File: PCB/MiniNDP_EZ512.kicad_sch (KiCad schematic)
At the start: 16 parts, among them J1 Conn_02x20_Odd_Even, U1 HC238, U2 HC4040, U3 FCT841, U4 AS6C4008, U5 HC00

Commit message: polish EZ512
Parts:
- C4: value 1u -> 47u; MPN CL31B105KAHNNNE -> C3216X5R1E476M160DC
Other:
- note added: "512K easy build"
- note removed: "NOT TESTED 512K easy build"
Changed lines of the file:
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@@
 	)
 	(junction
-		(at 119.38 162.56)
-		(diameter 0)
-		(color 0 0 0 0)
-	)
-	(junction
 		(at 127 147.32)
 		(diameter 0)
@@
 	)
 	(junction
+		(at 119.38 162.56)
+		(diameter 0)
+		(color 0 0 0 0)
+	)
+	(junction
 		(at 107.95 36.83)
 		(diameter 0)
@@
 	(wire
 		(pts
+			(xy 119.38 162.56) (xy 125.73 162.56)
+		)
+		(stroke
+			(width 0)
+			(type default)
+		)
+	)
+	(wire
+		(pts
 			(xy 34.29 41.91) (xy 44.45 41.91)
 		)
@@
 	(wire
 		(pts
-			(xy 114.3 167.64) (xy 119.38 167.64)
-		)
-		(stroke
-			(width 0)
-			(type default)
-		)
-	)
-	(wire
-		(pts
 			(xy 205.74 55.88) (xy 215.9 55.88)
 		)
@@
 		)
 	)
-	(wire
-		(pts
-			(xy 119.38 162.56) (xy 125.73 162.56)
-		)
-		(stroke
-			(width 0)
-			(type default)
-		)
-	)
 	(bus
 		(pts
@@
 	(wire
 		(pts
+			(xy 119.38 167.64) (xy 125.73 167.64)
+		)
+		(stroke
+			(width 0)
+			(type default)
+		)
+	)
+	(wire
+		(pts
 			(xy 241.3 68.58) (xy 257.81 68.58)
 		)
@@
 	(wire
 		(pts
-			(xy 119.38 167.64) (xy 125.73 167.64)
+			(xy 114.3 167.64) (xy 119.38 167.64)
 		)
 		(stroke
@@
 		)
 	)
-	(text "NOT TESTED\n512K easy build"
+	(text "512K easy build"
 		(exclude_from_sim no)
 		(at 261.112 173.99 0)
@@
 	)
 	(symbol
-		(lib_id "000_LOCAL:C")
-		(at 119.38 165.1 0)
-		(unit 1)
-		(exclude_from_sim no)
-		(in_bom yes)
-		(on_board yes)
-		(dnp no)
-		(property "Reference" "C4"
-			(at 119.38 158.75 0)
-			(effects
-				(font
-					(size 1.27 1.27)
-				)
-			)
-		)
-		(property "Value" "1u"
-			(at 119.38 161.036 0)
-			(effects
-				(font
-					(size 1.27 1.27)
-				)
-			)
-		)
-		(property "Footprint" "000_LOCAL:C_1206"
-			(at 119.38 165.1 0)
-			(effects
-				(font
-					(size 1.27 1.27)
-				)
-				(hide yes)
-			)
-		)
-		(property "Datasheet" "datasheets/CL05Y105KP6VPN.pdf"
-			(at 119.38 165.1 0)
-			(effects
-				(font
-					(size 1.27 1.27)
-				)
-				(hide yes)
-			)
-		)
-		(property "Description" "CAP CER 1UF 25V X7R 1206"
-			(at 119.38 165.1 0)
-			(effects
-				(font
-					(size 1.27 1.27)
-				)
-				(hide yes)
-			)
-		)
-		(property "MPN" "CL31B105KAHNNNE"
-			(at 119.38 165.1 0)
-			(effects
-				(font
-					(size 1.27 1.27)
-				)
-				(hide yes)
-			)
-		)
-		(pin "2"
-		)
-		(pin "1"
-		)
-		(instances
-			(project "MiniNDP_512_F"
-				(path "/f15c2929-5cf4-4b4e-965d-148e1bec8a42"
-					(reference "C4")
-					(unit 1)
-				)
-			)
-		)
-	)
-	(symbol
 		(lib_id "power:VBUS")
 		(at 68.58 85.09 0)
@@
 					(unit 1)
 				)
+			)
+		)
+	)
+	(symbol
+		(lib_id "000_LOCAL:C")
+		(at 119.38 165.1 0)
+		(unit 1)
+		(exclude_from_sim no)
+		(in_bom yes)
+		(on_board yes)
+		(dnp no)
+		(property "Reference" "C4"
+			(at 119.38 158.75 0)
+			(effects
+				(font
+					(size 1.27 1.27)
+				)
+			)
+		)
+		(property "Value" "47u"
+			(at 119.38 161.036 0)
+			(effects
+				(font
+					(size 1.27 1.27)
+				)
+			)
+		)
+		(property "Footprint" "000_LOCAL:C_1206"
+			(at 119.38 165.1 0)
+			(effects
+				(font
+					(size 1.27 1.27)
+				)
+				(hide yes)
+			)
+		)
+		(property "Datasheet" "datasheets/TDK_MLCC_Cxxxx.pdf"
+			(at 119.38 165.1 0)
+			(effects
+				(font
+					(size 1.27 1.27)
+				)
+				(hide yes)
+			)
+		)
+		(property "Description" "CAP CER 47UF 25V X5R 1206"
+			(at 119.38 165.1 0)
+			(effects
+				(font
+					(size 1.27 1.27)
+				)
+				(hide yes)
+			)
+		)
+		(property "MPN" "C3216X5R1E476M160DC"
+			(at 119.38 165.1 0)
+			(effects
+				(font
+					(size 1.27 1.27)
+				)
+				(hide yes)
+			)
+		)
+		(pin "2"
+		)
+		(pin "1"
+		)
+		(instances
+			(project "MiniNDP_EZ512"
+				(path "/f15c2929-5cf4-4b4e-965d-148e1bec8a42"
+					(reference "C4")
+					(unit 1)
+				)

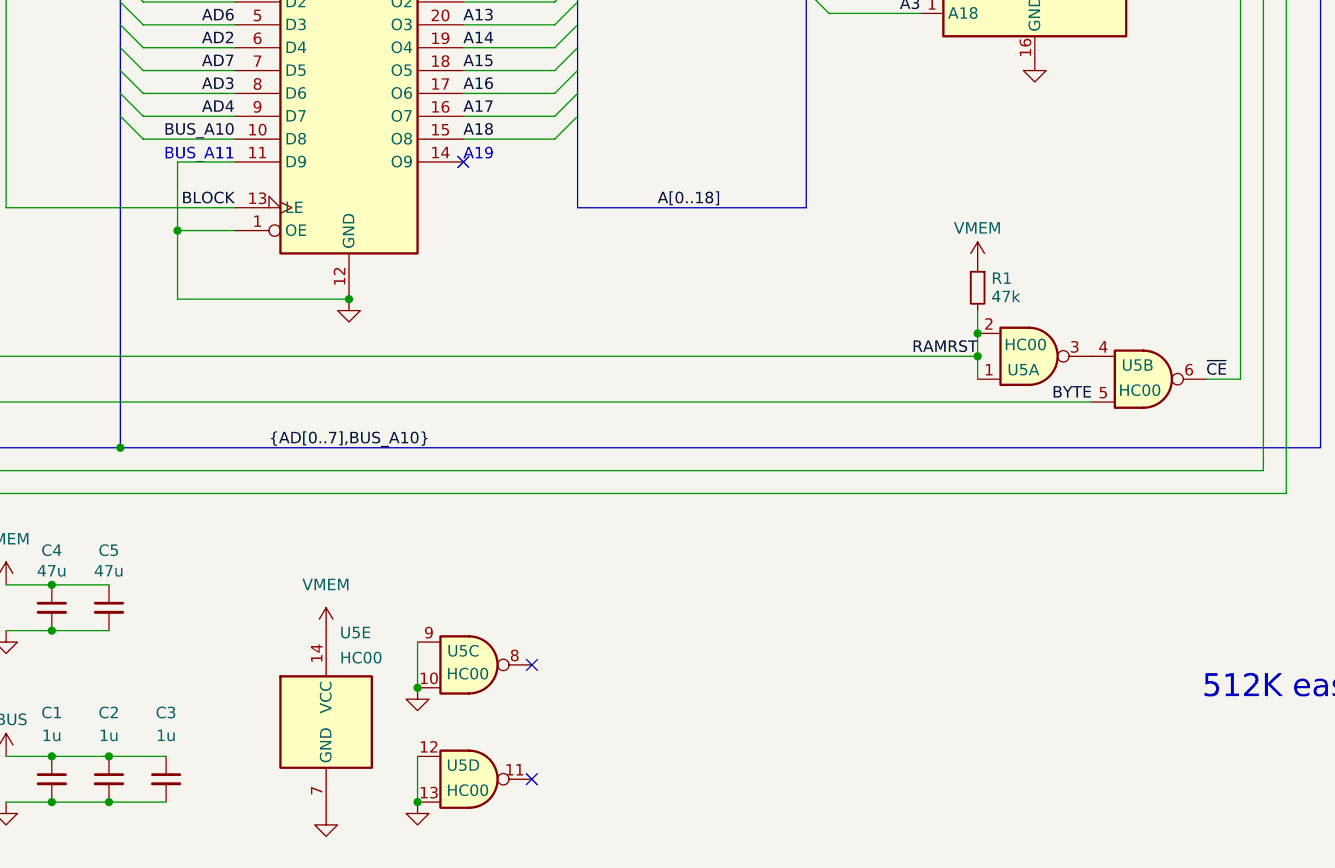
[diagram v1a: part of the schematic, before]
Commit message: embed code font in pcb, bom export filename variables, delete extra battery trace
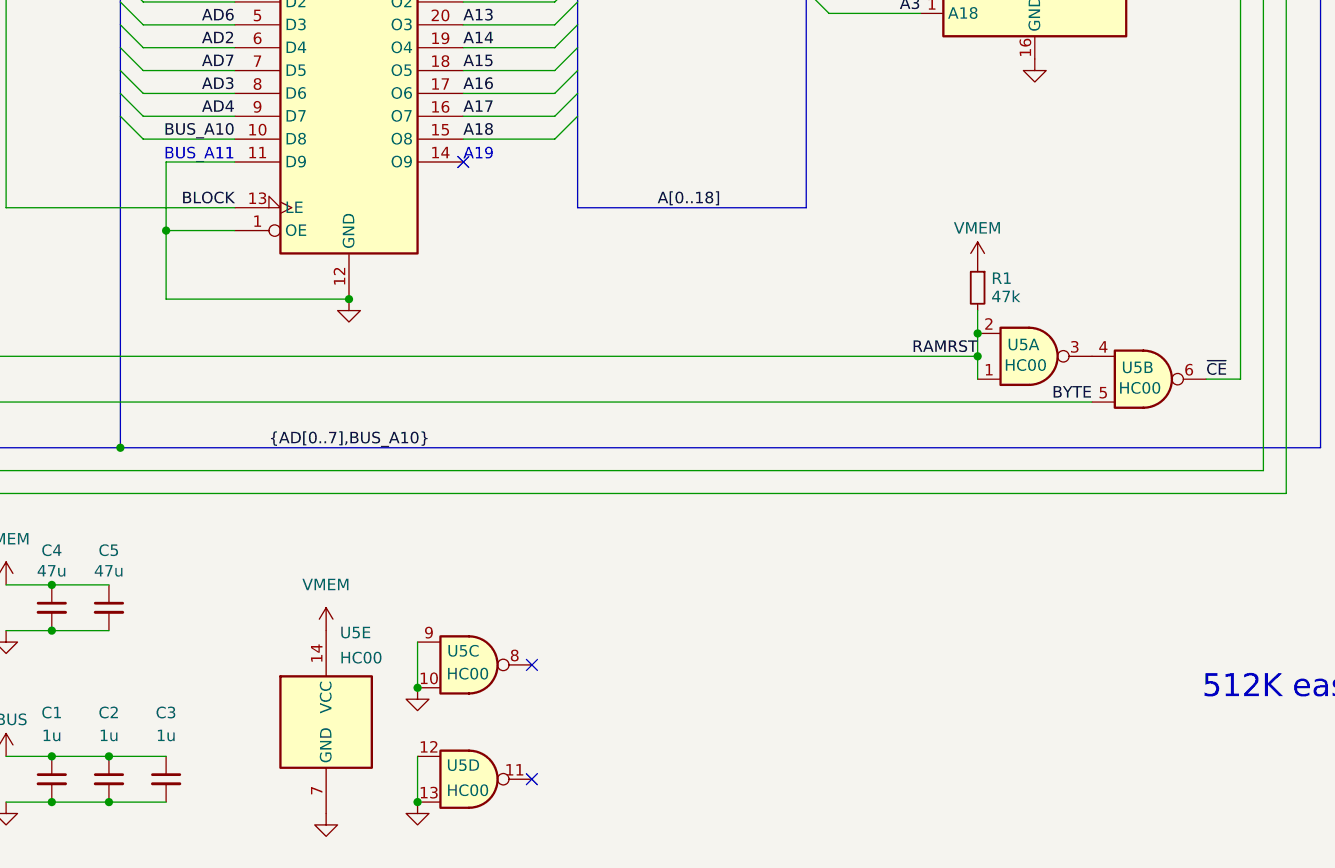
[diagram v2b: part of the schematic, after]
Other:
- title: MiniNDP -> MiniNDP_EZ512
